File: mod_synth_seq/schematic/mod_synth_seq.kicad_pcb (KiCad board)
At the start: 2 copper layers, 87 parts, among them J1 CV1, J10 Step 8 Gate, J11 Reset, J12 Clock, J13 Gate Out, J2 CV2, J3 Step 1 Gate, J4 Step 2 Gate, J5 Step 3 Gate, J6 Step 4 Gate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

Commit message: Start to layout seq PCB
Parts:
- moved D1 147.6 mm to (64.8, 27.9)
- moved D9 135.0 mm to (85.1, 27.9)
- moved D5 134.6 mm to (74.9, 27.9)
- moved D17 111.0 mm to (105.4, 27.9)
- moved D21 104.1 mm to (115.6, 27.9)
- moved D25 95.0 mm to (125.7, 27.9)
- moved D29 90.2 mm to (135.9, 27.9)
- moved D13 70.2 mm to (95.2, 27.9)
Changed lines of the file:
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@@
   )
   (module LED_THT:LED_D5.0mm (layer F.Cu)
-    (at 208.67 81.16)
+    (at 135.89 27.94)
     (descr "LED, diameter 5.0mm, 2 pins, http://cdn-reichelt.de/documents/datenblatt/A500/LL-504BC2E-009.pdf")
     (tags "LED diameter 5.0mm 2 pins")
@@
   )
   (module LED_THT:LED_D5.0mm (layer F.Cu)
-    (at 193.87 94.2)
+    (at 125.73 27.94)
     (descr "LED, diameter 5.0mm, 2 pins, http://cdn-reichelt.de/documents/datenblatt/A500/LL-504BC2E-009.pdf")
     (tags "LED diameter 5.0mm 2 pins")
@@
   )
   (module LED_THT:LED_D5.0mm (layer F.Cu)
-    (at 169.02 117.25)
+    (at 115.57 27.94)
     (descr "LED, diameter 5.0mm, 2 pins, http://cdn-reichelt.de/documents/datenblatt/A500/LL-504BC2E-009.pdf")
     (tags "LED diameter 5.0mm 2 pins")
@@
   )
   (module LED_THT:LED_D5.0mm (layer F.Cu)
-    (at 186.8 103.38)
+    (at 105.41 27.94)
     (descr "LED, diameter 5.0mm, 2 pins, http://cdn-reichelt.de/documents/datenblatt/A500/LL-504BC2E-009.pdf")
     (tags "LED diameter 5.0mm 2 pins")
@@
   )
   (module LED_THT:LED_D5.0mm (layer F.Cu)
-    (at 103.8 97.61)
+    (at 95.25 27.94)
     (descr "LED, diameter 5.0mm, 2 pins, http://cdn-reichelt.de/documents/datenblatt/A500/LL-504BC2E-009.pdf")
     (tags "LED diameter 5.0mm 2 pins")
@@
   )
   (module LED_THT:LED_D5.0mm (layer F.Cu)
-    (at 204.64 90.65)
+    (at 85.09 27.94)
     (descr "LED, diameter 5.0mm, 2 pins, http://cdn-reichelt.de/documents/datenblatt/A500/LL-504BC2E-009.pdf")
     (tags "LED diameter 5.0mm 2 pins")
@@
   )
   (module LED_THT:LED_D5.0mm (layer F.Cu)
-    (at 176.52 116.25)
+    (at 74.93 27.94)
     (descr "LED, diameter 5.0mm, 2 pins, http://cdn-reichelt.de/documents/datenblatt/A500/LL-504BC2E-009.pdf")
     (tags "LED diameter 5.0mm 2 pins")
@@
   )
   (module LED_THT:LED_D5.0mm (layer F.Cu)
-    (at 186.8 110.93)
+    (at 64.77 27.94)
     (descr "LED, diameter 5.0mm, 2 pins, http://cdn-reichelt.de/documents/datenblatt/A500/LL-504BC2E-009.pdf")
     (tags "LED diameter 5.0mm 2 pins")

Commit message: Rough layout for seq
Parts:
- moved D4 175.4 mm to (34.3, 101.6)
- moved R3 166.0 mm to (33.0, 25.4)
- moved D6 161.4 mm to (47.0, 58.4)
- moved R6 152.2 mm to (47.0, 108.0)
- moved R5 146.5 mm to (48.3, 25.4)
- moved D8 144.0 mm to (49.5, 101.6)
- moved D2 143.6 mm to (30.5, 58.4)
- moved RV2 142.6 mm to (35.6, 76.2), turned to 90 degrees
- moved R8 136.4 mm to (62.2, 108.0)
- moved D3 132.9 mm to (30.5, 82.5)
- moved RV4 131.5 mm to (52.1, 76.2), turned to 90 degrees
- moved R7 130.9 mm to (63.5, 25.4)
- moved D7 130.5 mm to (47.0, 82.5)
- moved D10 120.4 mm to (63.5, 58.4)
- moved R4 119.5 mm to (31.8, 108.0)
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
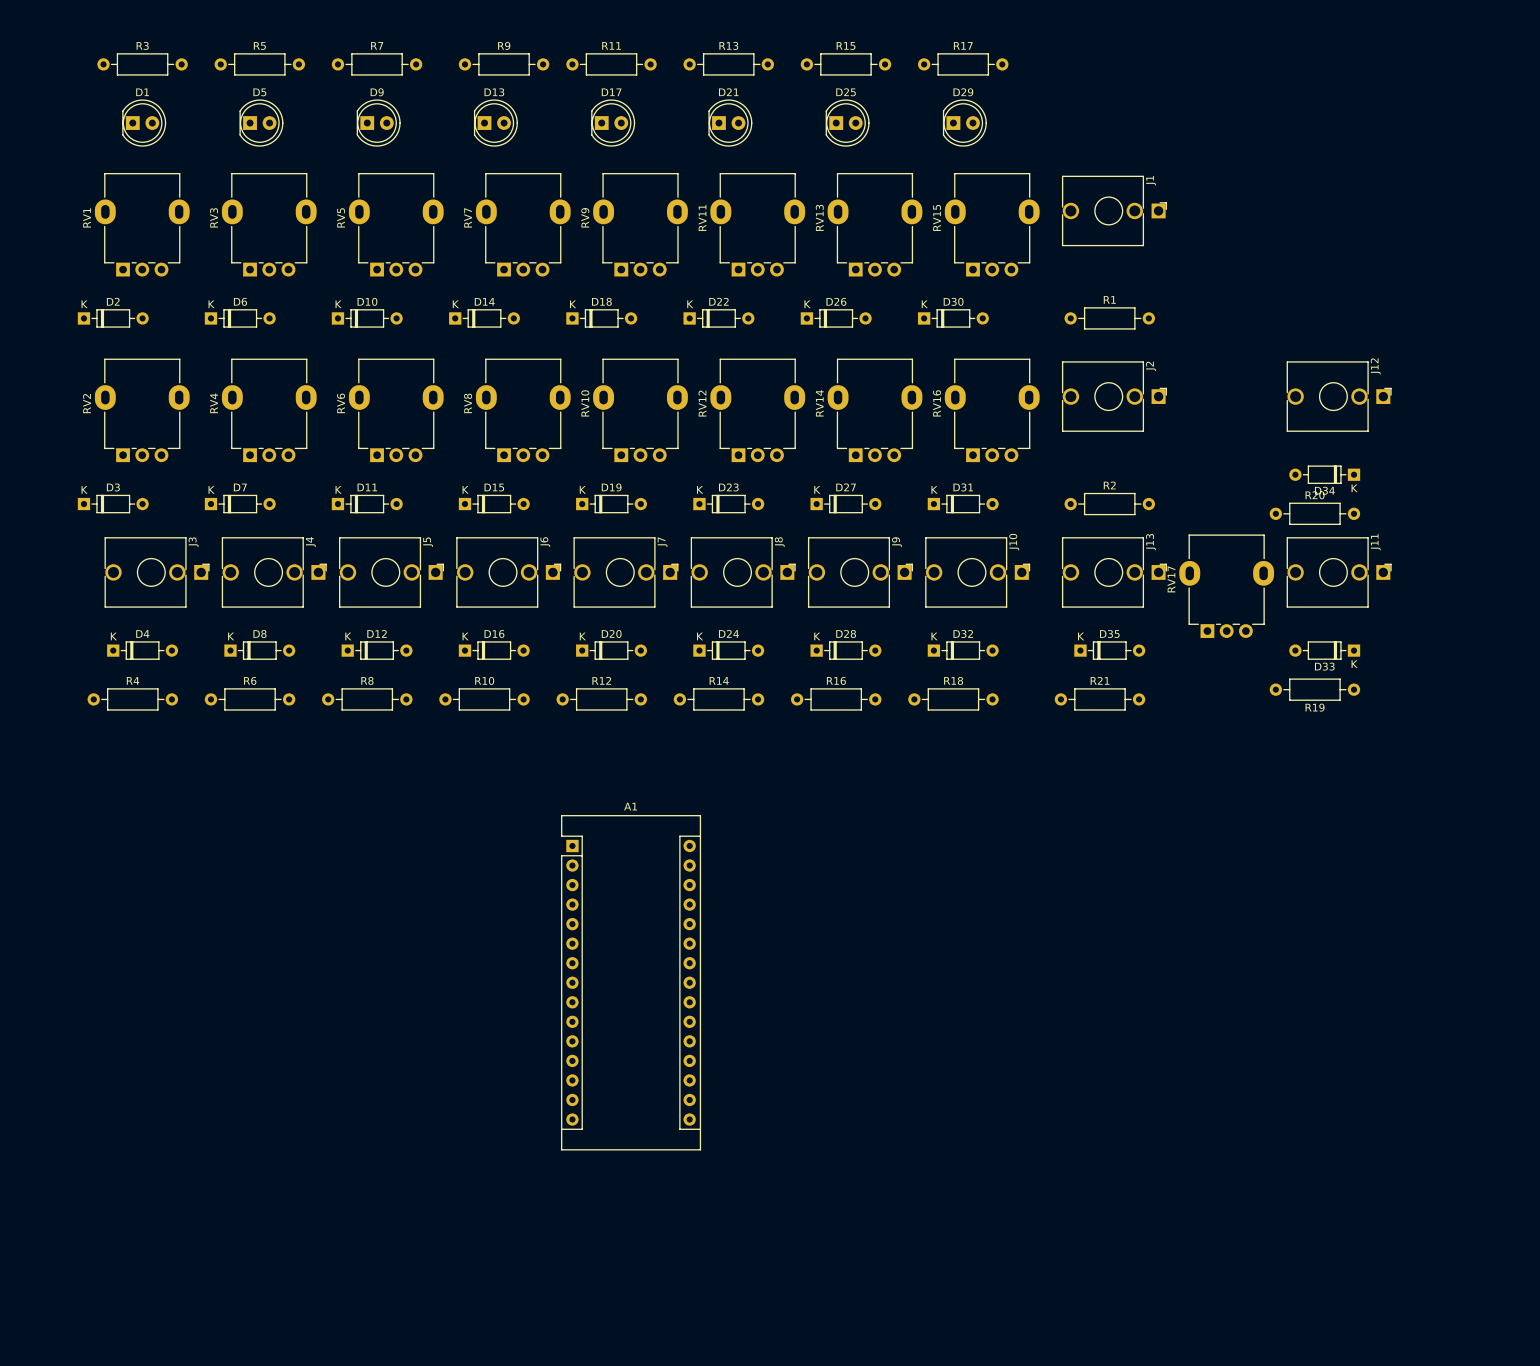
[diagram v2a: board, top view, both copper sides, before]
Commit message: Add 3u 28hp dimensions to seq
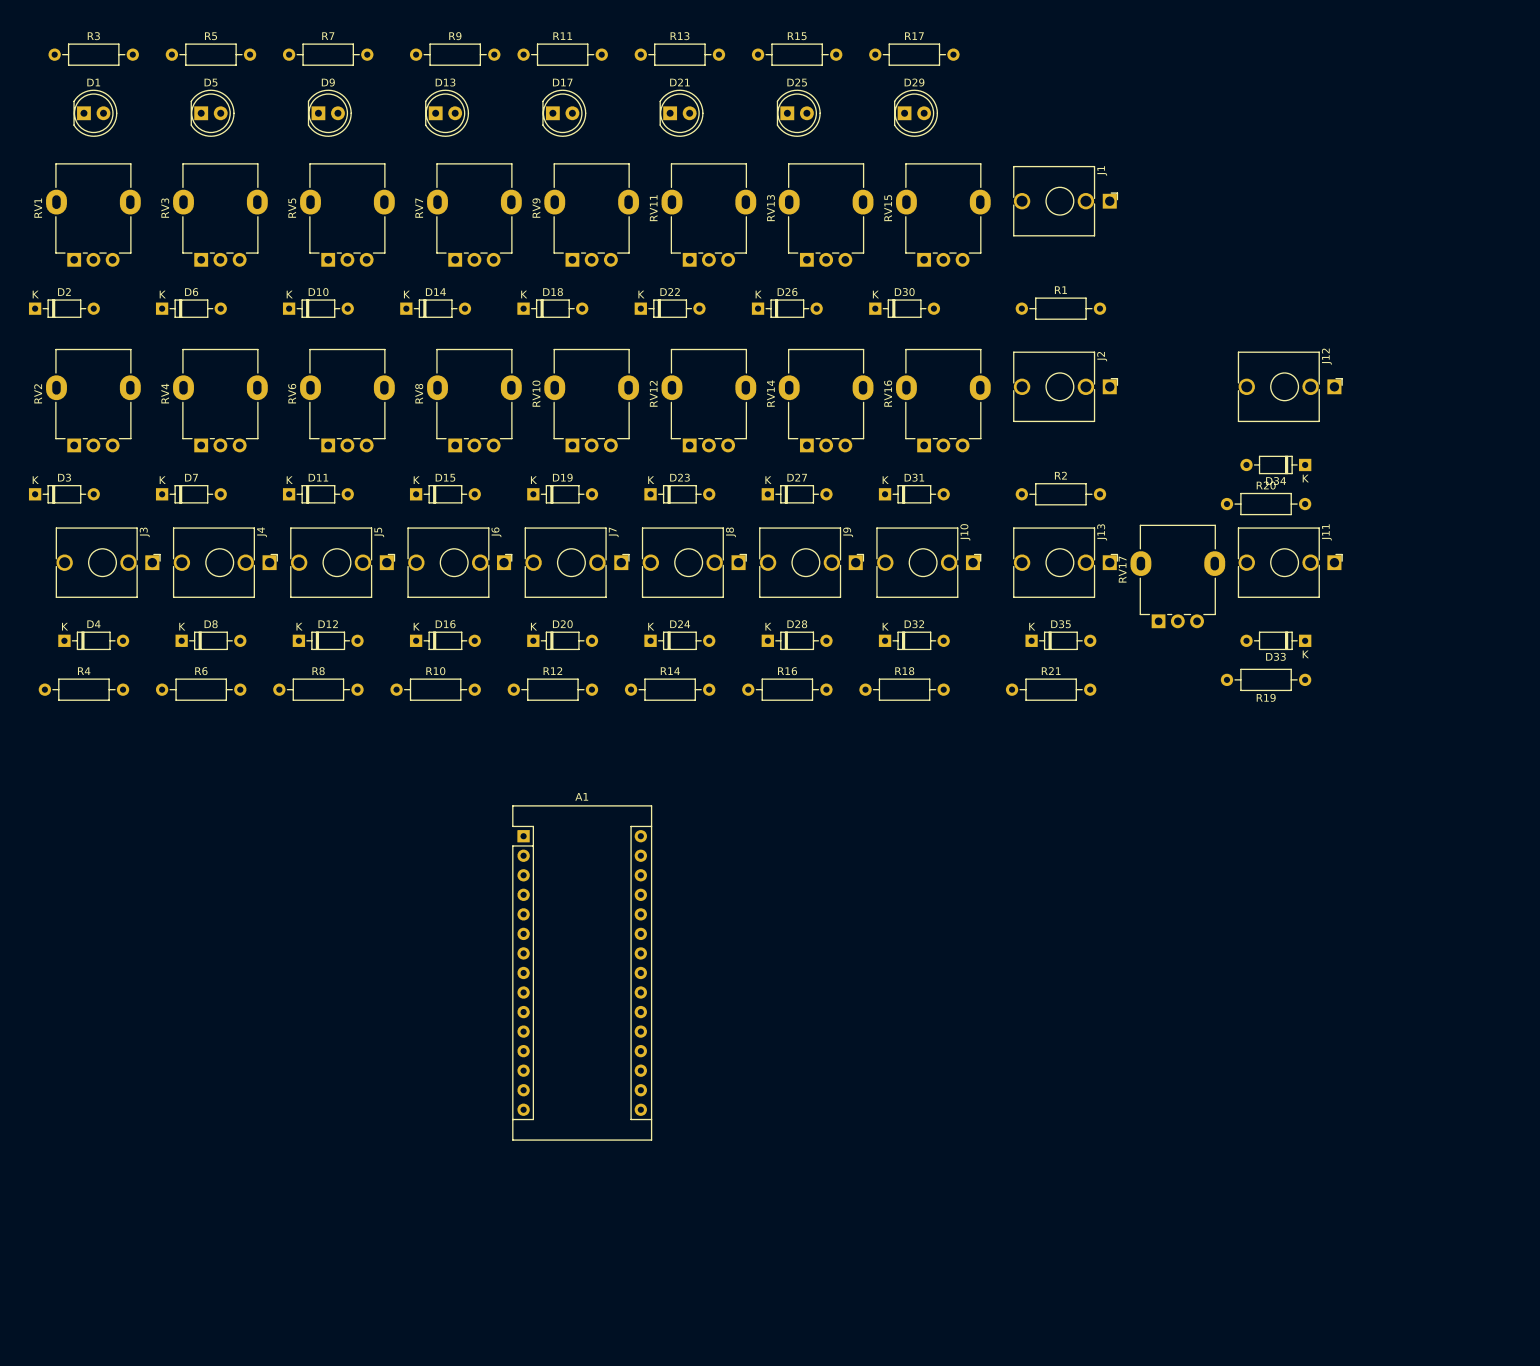
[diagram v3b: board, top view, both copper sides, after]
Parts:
- moved R19 6.48 mm to (189.2, 105.4)
- moved RV15 6.48 mm to (139.7, 50.8)
- moved D33 6.48 mm to (189.2, 100.3)
- moved D34 6.48 mm to (189.2, 77.5)
- moved D35 6.48 mm to (153.7, 100.3)
- moved RV16 6.48 mm to (139.7, 74.9)
- moved D17 6.48 mm to (91.4, 31.8)
- moved D18 6.48 mm to (87.6, 57.1)
- moved D25 6.48 mm to (121.9, 31.8)
- moved RV13 6.48 mm to (124.5, 50.8)
- moved RV7 6.48 mm to (78.7, 50.8)
- moved A1 6.48 mm to (87.6, 125.7)
- moved D15 6.48 mm to (73.7, 81.3)
- moved D16 6.48 mm to (73.7, 100.3)
- moved D27 6.48 mm to (119.4, 81.3)
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
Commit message: Start to reorganise layout
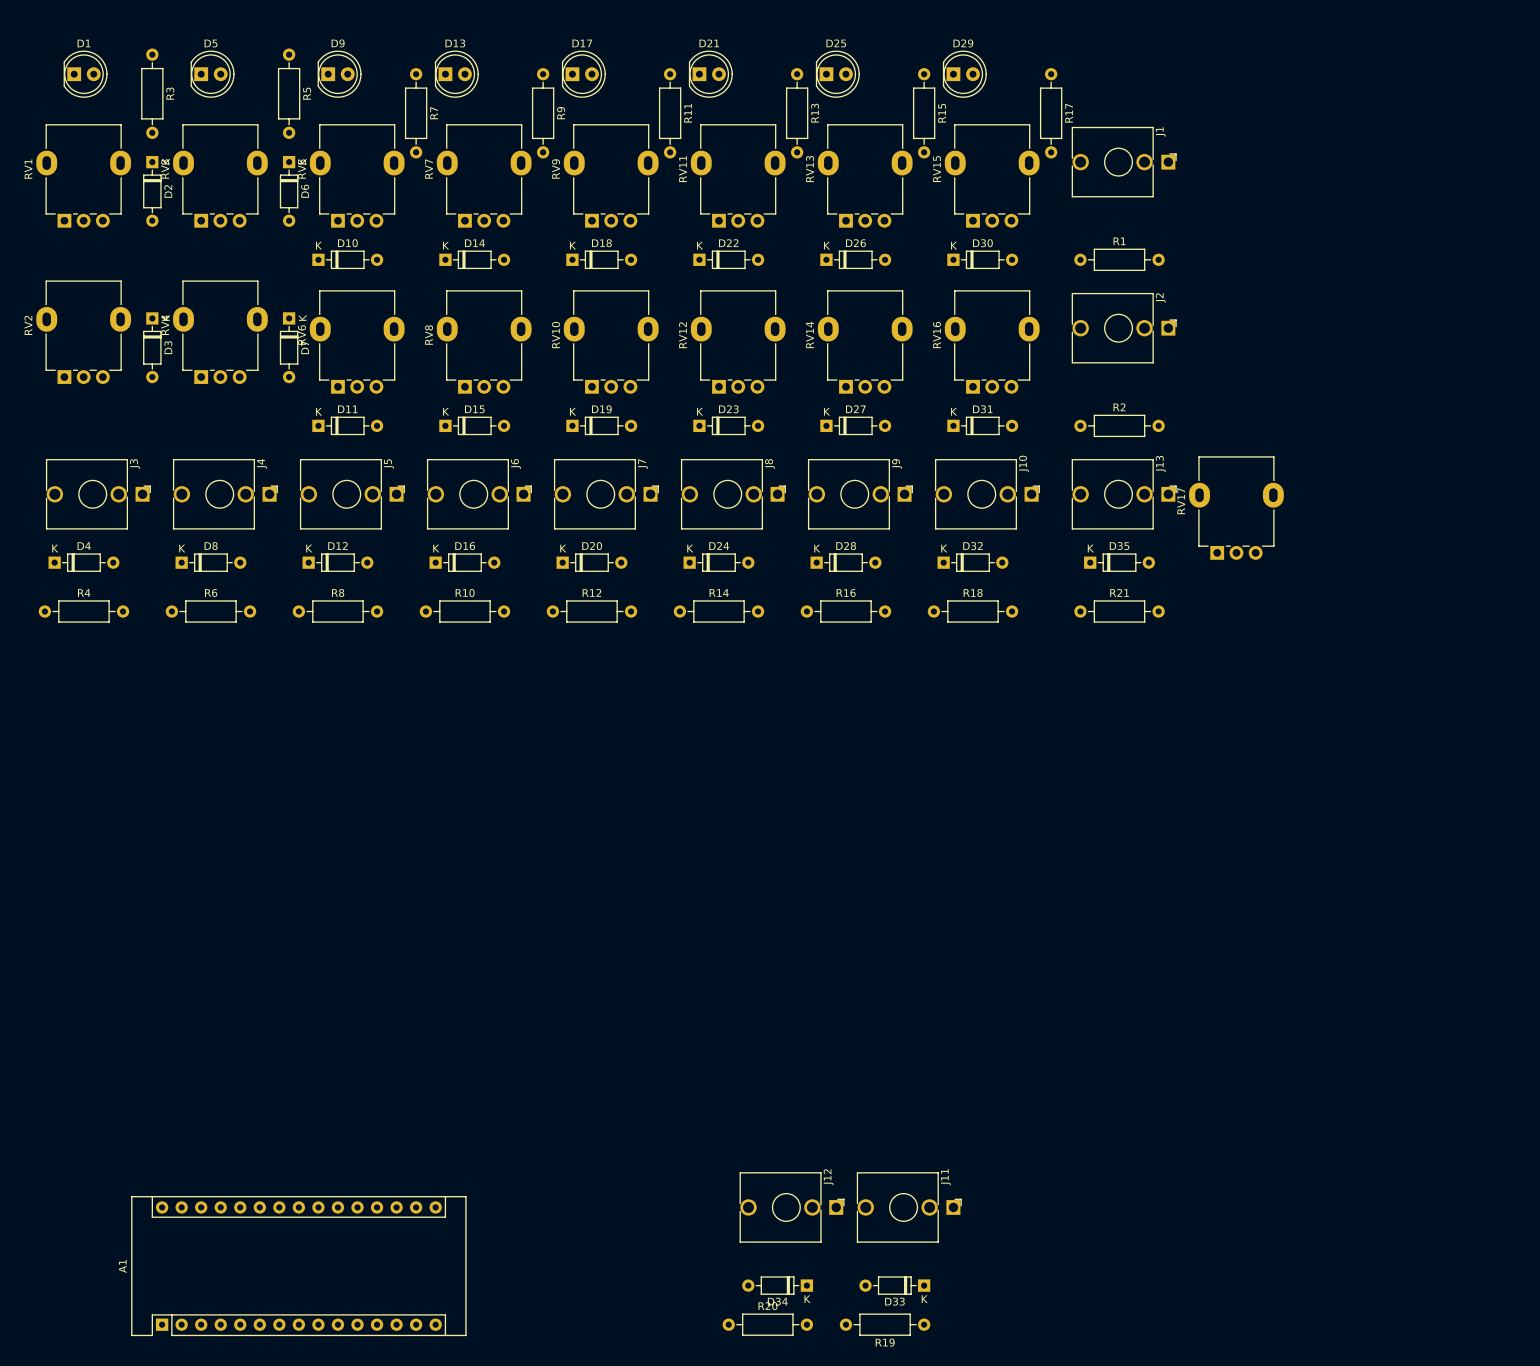
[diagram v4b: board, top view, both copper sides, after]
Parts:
- moved D34 124.8 mm to (124.5, 184.2)
- moved J12 124.8 mm to (128.3, 174.0)
- moved R20 124.8 mm to (114.3, 189.2)
- moved D33 97.4 mm to (139.7, 184.2)
- moved J11 97.4 mm to (143.5, 174.0)
- moved R19 97.4 mm to (139.7, 189.2)
- moved A1 79.0 mm to (40.6, 189.2), turned to 90 degrees
- moved D7 28.2 mm to (57.1, 58.4), turned to 270 degrees
- moved D3 27.5 mm to (39.4, 58.4), turned to 270 degrees
- moved D6 25.2 mm to (57.1, 38.1), turned to 270 degrees
- moved D2 24.4 mm to (39.4, 38.1), turned to 270 degrees
- moved R17 23.0 mm to (156.2, 26.7), turned to 270 degrees
- moved R15 21.7 mm to (139.7, 26.7), turned to 270 degrees
- moved R13 20.5 mm to (123.2, 26.7), turned to 270 degrees
- moved R11 19.2 mm to (106.7, 26.7), turned to 270 degrees
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
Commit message: Attempt to lay some tracks
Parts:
- added REF**: IDC-Header_2x08_P2.54mm_Vertical, Connector_IDC:IDC-Header_2x08_P2.54mm_Vertical, F.Cu at (97.8, 92.7)
- moved A1 145.3 mm to (115.6, 64.8), turned to 180 degrees
- moved D34 132.8 mm to (110.5, 52.1)
- moved R20 123.2 mm to (113.0, 66.0), turned to 180 degrees
- moved D33 118.0 mm to (110.5, 69.8)
- moved J12 116.4 mm to (114.3, 58.4)
- moved R19 108.7 mm to (113.0, 83.8)
- moved J11 102.1 mm to (114.3, 76.2)
- moved RV9 94.3 mm to (27.9, 110.5)
- moved RV10 93.5 mm to (27.9, 130.8)
- moved RV11 93.4 mm to (45.7, 110.5)
- moved RV12 92.5 mm to (45.7, 130.8)
- moved RV13 92.5 mm to (63.5, 110.5)
- moved R11 91.7 mm to (39.4, 88.9)
- moved RV14 91.6 mm to (63.5, 130.8)
- moved D17 91.6 mm to (29.2, 91.4)
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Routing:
- net GND: track 0.00 -> 462.3 mm
- net Net-(D11-Pad1): track 0.00 -> 273.4 mm
- net Net-(A1-Pad7): track 0.00 -> 65.7 mm
- net Net-(A1-Pad11): track 0.00 -> 65.7 mm
- net Net-(A1-Pad9): track 0.00 -> 65.7 mm
- net Net-(A1-Pad8): track 0.00 -> 65.7 mm
- net Net-(A1-Pad6): track 0.00 -> 65.7 mm
- net Net-(A1-Pad5): track 0.00 -> 65.7 mm
- net Net-(A1-Pad12): track 0.00 -> 65.7 mm
- net Net-(A1-Pad10): track 0.00 -> 65.7 mm
- net Net-(D10-Pad1): track 0.00 -> 35.6 mm
- net Net-(D35-Pad1): track 0.00 -> 24.1 mm
- net Net-(D32-Pad2): track 0.00 -> 15.0 mm
- net Net-(D28-Pad2): track 0.00 -> 15.0 mm
- net Net-(D24-Pad2): track 0.00 -> 15.0 mm
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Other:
- board outline added: 100.3 x 132.1 mm
